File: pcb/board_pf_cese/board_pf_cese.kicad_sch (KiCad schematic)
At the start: 13 parts, among them J1 Screw_Terminal_01x02, J2 Conn_01x04, J3 Conn_01x04, J4 Conn_01x04, J5 Conn_01x04, J6 Conn_01x15, J7 Conn_01x15, J8 Conn_01x08, J9 Conn_01x08

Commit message: colocacion de componentes en el pcb
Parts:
- D1, D2: footprint (none) -> LED_THT:LED_D3.0mm
- J1: footprint (none) -> TerminalBlock_Phoenix:TerminalBlock_Phoenix_MPT-0,5-2-2.54_1x02_P2.54mm_Horizontal
- J2, J3, J4, J5: footprint (none) -> Connector_PinSocket_2.54mm:PinSocket_1x04_P2.54mm_Vertical
- J6, J7: footprint (none) -> Connector_PinSocket_2.54mm:PinSocket_1x15_P2.54mm_Vertical
- J8, J9: footprint (none) -> Connector_PinSocket_2.54mm:PinSocket_1x08_P2.54mm_Vertical
- R1, R2: footprint (none) -> Resistor_THT:R_Axial_DIN0207_L6.3mm_D2.5mm_P10.16mm_Horizontal
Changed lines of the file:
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@@
     (property "Reference" "J3" (id 0) (at 52.07 105.41 0))
     (property "Value" "Conn_01x04" (id 1) (at 52.07 107.95 0))
-    (property "Footprint" "" (id 2) (at 52.07 114.3 0)
+    (property "Footprint" "Connector_PinSocket_2.54mm:PinSocket_1x04_P2.54mm_Vertical" (id 2) (at 52.07 114.3 0)
       (effects (font (size 1.27 1.27)) hide)
     )
@@
     (property "Reference" "J5" (id 0) (at 52.07 153.67 0))
     (property "Value" "Conn_01x04" (id 1) (at 52.07 156.21 0))
-    (property "Footprint" "" (id 2) (at 52.07 162.56 0)
+    (property "Footprint" "Connector_PinSocket_2.54mm:PinSocket_1x04_P2.54mm_Vertical" (id 2) (at 52.07 162.56 0)
       (effects (font (size 1.27 1.27)) hide)
     )
@@
     (property "Reference" "J9" (id 0) (at 247.65 35.56 0))
     (property "Value" "Conn_01x08" (id 1) (at 247.65 38.1 0))
-    (property "Footprint" "" (id 2) (at 247.65 49.53 0)
+    (property "Footprint" "Connector_PinSocket_2.54mm:PinSocket_1x08_P2.54mm_Vertical" (id 2) (at 247.65 49.53 0)
       (effects (font (size 1.27 1.27)) hide)
     )
@@
     (property "Reference" "J1" (id 0) (at 38.1 34.29 0))
     (property "Value" "Screw_Terminal_01x02" (id 1) (at 38.1 36.83 0))
-    (property "Footprint" "" (id 2) (at 38.1 40.64 0)
+    (property "Footprint" "TerminalBlock_Phoenix:TerminalBlock_Phoenix_MPT-0,5-2-2.54_1x02_P2.54mm_Horizontal" (id 2) (at 38.1 40.64 0)
       (effects (font (size 1.27 1.27)) hide)
     )
@@
     (property "Reference" "J4" (id 0) (at 52.07 129.54 0))
     (property "Value" "Conn_01x04" (id 1) (at 52.07 132.08 0))
-    (property "Footprint" "" (id 2) (at 52.07 137.16 0)
+    (property "Footprint" "Connector_PinSocket_2.54mm:PinSocket_1x04_P2.54mm_Vertical" (id 2) (at 52.07 137.16 0)
       (effects (font (size 1.27 1.27)) hide)
     )
@@
       (effects (font (size 1.27 1.27)) (justify left))
     )
-    (property "Footprint" "" (id 2) (at 134.62 62.23 0)
+    (property "Footprint" "Connector_PinSocket_2.54mm:PinSocket_1x15_P2.54mm_Vertical" (id 2) (at 134.62 62.23 0)
       (effects (font (size 1.27 1.27)) hide)
     )
@@
       (effects (font (size 1.27 1.27)) (justify left))
     )
-    (property "Footprint" "" (id 2) (at 229.87 49.53 0)
+    (property "Footprint" "Connector_PinSocket_2.54mm:PinSocket_1x08_P2.54mm_Vertical" (id 2) (at 229.87 49.53 0)
       (effects (font (size 1.27 1.27)) hide)
     )
@@
     (property "Reference" "J7" (id 0) (at 149.86 38.1 0))
     (property "Value" "Conn_01x15" (id 1) (at 149.86 40.64 0))
-    (property "Footprint" "" (id 2) (at 149.86 62.23 0)
+    (property "Footprint" "Connector_PinSocket_2.54mm:PinSocket_1x15_P2.54mm_Vertical" (id 2) (at 149.86 62.23 0)
       (effects (font (size 1.27 1.27)) hide)
     )
@@
       (effects (font (size 1.27 1.27)) (justify right))
     )
-    (property "Footprint" "" (id 2) (at 231.14 123.19 0)
+    (property "Footprint" "LED_THT:LED_D3.0mm" (id 2) (at 231.14 123.19 0)
       (effects (font (size 1.27 1.27)) hide)
     )
@@
       (effects (font (size 1.27 1.27)) (justify left))
     )
-    (property "Footprint" "" (id 2) (at 229.362 111.76 90)
+    (property "Footprint" "Resistor_THT:R_Axial_DIN0207_L6.3mm_D2.5mm_P10.16mm_Horizontal" (id 2) (at 229.362 111.76 90)
       (effects (font (size 1.27 1.27)) hide)
     )
@@
     (property "Reference" "J2" (id 0) (at 52.07 81.28 0))
     (property "Value" "Conn_01x04" (id 1) (at 52.07 83.82 0))
-    (property "Footprint" "" (id 2) (at 52.07 90.17 0)
+    (property "Footprint" "Connector_PinSocket_2.54mm:PinSocket_1x04_P2.54mm_Vertical" (id 2) (at 52.07 90.17 0)
       (effects (font (size 1.27 1.27)) hide)
     )
@@
       (effects (font (size 1.27 1.27)) (justify right))
     )
-    (property "Footprint" "" (id 2) (at 245.11 123.19 0)
+    (property "Footprint" "LED_THT:LED_D3.0mm" (id 2) (at 245.11 123.19 0)
       (effects (font (size 1.27 1.27)) hide)
     )
@@
       (effects (font (size 1.27 1.27)) (justify left))
     )
-    (property "Footprint" "" (id 2) (at 243.332 111.76 90)
+    (property "Footprint" "Resistor_THT:R_Axial_DIN0207_L6.3mm_D2.5mm_P10.16mm_Horizontal" (id 2) (at 243.332 111.76 90)
       (effects (font (size 1.27 1.27)) hide)
     )
@@
     )
     (path "/c2c16862-67ff-42a4-afba-5ce90d66562f"
-      (reference "D1") (unit 1) (value "LED") (footprint "")
+      (reference "D1") (unit 1) (value "LED") (footprint "LED_THT:LED_D3.0mm")
     )
     (path "/dbc81720-7b11-4359-846d-7205cd8fe101"
-      (reference "D2") (unit 1) (value "LED") (footprint "")
+      (reference "D2") (unit 1) (value "LED") (footprint "LED_THT:LED_D3.0mm")
     )
     (path "/587a09bb-470b-457f-a0a3-250ad0d2fb36"
-      (reference "J1") (unit 1) (value "Screw_Terminal_01x02") (footprint "")
+      (reference "J1") (unit 1) (value "Screw_Terminal_01x02") (footprint "TerminalBlock_Phoenix:TerminalBlock_Phoenix_MPT-0,5-2-2.54_1x02_P2.54mm_Horizontal")
     )
     (path "/d8bb4505-4a60-4c8e-93d0-f0d006cbd6be"
-      (reference "J2") (unit 1) (value "Conn_01x04") (footprint "")
+      (reference "J2") (unit 1) (value "Conn_01x04") (footprint "Connector_PinSocket_2.54mm:PinSocket_1x04_P2.54mm_Vertical")
     )
     (path "/10d63046-38df-4d8c-a6ed-2c840220c859"
-      (reference "J3") (unit 1) (value "Conn_01x04") (footprint "")
+      (reference "J3") (unit 1) (value "Conn_01x04") (footprint "Connector_PinSocket_2.54mm:PinSocket_1x04_P2.54mm_Vertical")
     )
     (path "/6a61e119-9f63-4329-8362-52b2b0488a19"
-      (reference "J4") (unit 1) (value "Conn_01x04") (footprint "")
+      (reference "J4") (unit 1) (value "Conn_01x04") (footprint "Connector_PinSocket_2.54mm:PinSocket_1x04_P2.54mm_Vertical")
     )
     (path "/36055566-6b01-4db2-9bbc-8bfca51561a0"
-      (reference "J5") (unit 1) (value "Conn_01x04") (footprint "")
+      (reference "J5") (unit 1) (value "Conn_01x04") (footprint "Connector_PinSocket_2.54mm:PinSocket_1x04_P2.54mm_Vertical")
     )
     (path "/97707070-82f5-4b99-9a61-dd439405b8e4"
-      (reference "J6") (unit 1) (value "Conn_01x15") (footprint "")
+      (reference "J6") (unit 1) (value "Conn_01x15") (footprint "Connector_PinSocket_2.54mm:PinSocket_1x15_P2.54mm_Vertical")
     )
     (path "/b19ccc00-1834-4ad9-8a41-194837d21601"
-      (reference "J7") (unit 1) (value "Conn_01x15") (footprint "")
+      (reference "J7") (unit 1) (value "Conn_01x15") (footprint "Connector_PinSocket_2.54mm:PinSocket_1x15_P2.54mm_Vertical")
     )
     (path "/9785fda7-cab3-4d47-9212-e11d694f5957"
-      (reference "J8") (unit 1) (value "Conn_01x08") (footprint "")
+      (reference "J8") (unit 1) (value "Conn_01x08") (footprint "Connector_PinSocket_2.54mm:PinSocket_1x08_P2.54mm_Vertical")
     )
     (path "/49eaddac-835c-4189-b730-464b8007ff04"
-      (reference "J9") (unit 1) (value "Conn_01x08") (footprint "")
+      (reference "J9") (unit 1) (value "Conn_01x08") (footprint "Connector_PinSocket_2.54mm:PinSocket_1x08_P2.54mm_Vertical")
     )
     (path "/caddb6f5-1981-41a3-8e50-483141adabfe"
-      (reference "R1") (unit 1) (value "R") (footprint "")
+      (reference "R1") (unit 1) (value "R") (footprint "Resistor_THT:R_Axial_DIN0207_L6.3mm_D2.5mm_P10.16mm_Horizontal")
     )
     (path "/f10d6887-62d2-486c-8b5f-1063e4909e37"
-      (reference "R2") (unit 1) (value "R") (footprint "")
-    )
-  )
+      (reference "R2") (unit 1) (value "R") (footprint "Resistor_THT:R_Axial_DIN0207_L6.3mm_D2.5mm_P10.16mm_Horizontal")
+    )
+  )

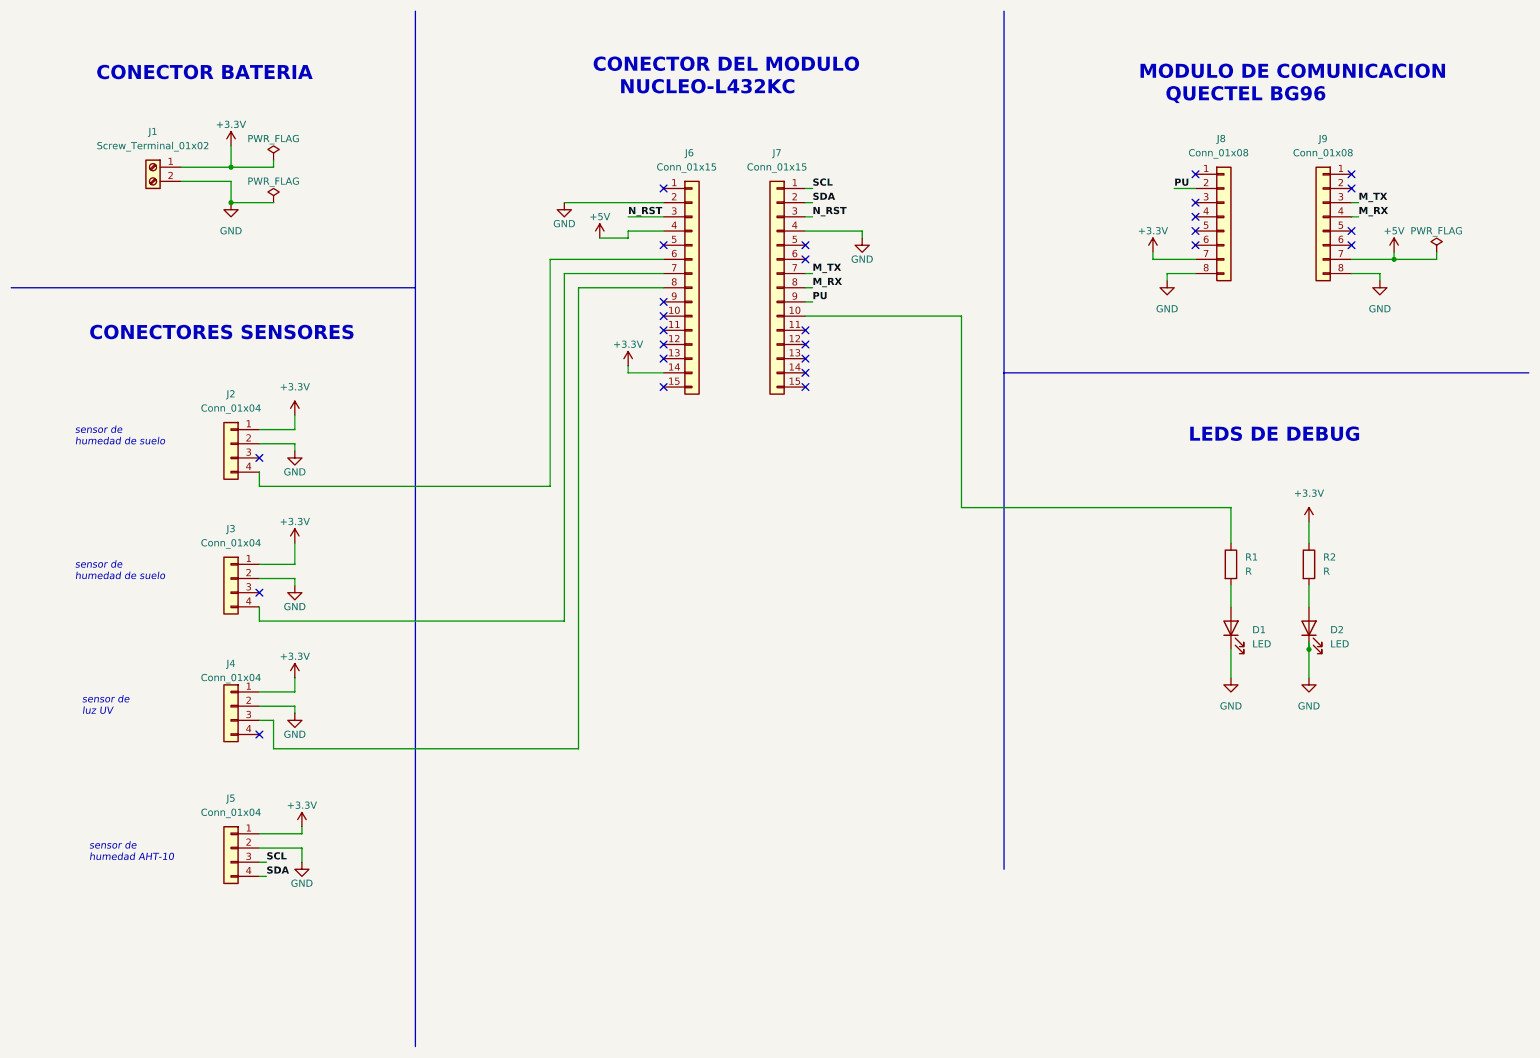
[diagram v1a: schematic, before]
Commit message: se redimensiono el tamaño del pcb
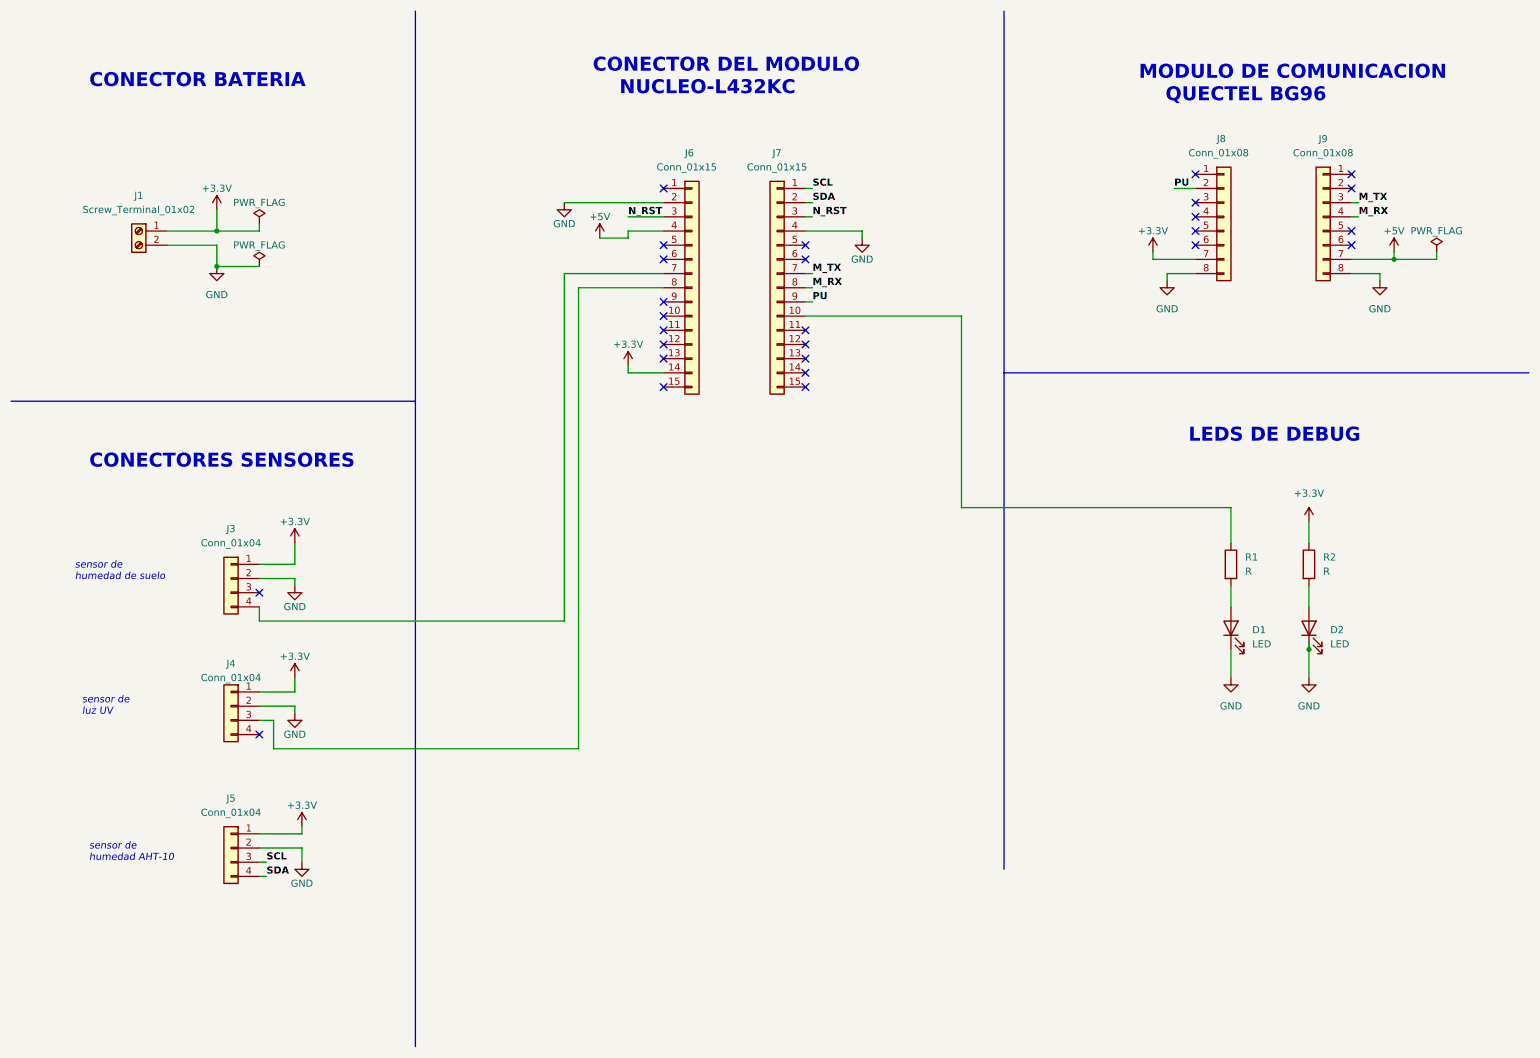
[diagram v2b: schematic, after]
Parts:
- removed J2: Conn_01x04, Connector_PinSocket_2.54mm:PinSocket_1x04_P2.54mm_Vertical, symbol Connector_Generic:Conn_01x04
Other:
- moved on the sheet: J1

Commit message: ruteo con errores
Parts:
- added J2: Conn_01x04, Connector_PinSocket_2.54mm:PinSocket_1x04_P2.54mm_Vertical, symbol Connector_Generic:Conn_01x04
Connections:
- net +3.3V: now also J2.1 (Pin_1); no longer R2.1
- net GND: now also J2.2 (Pin_2)
- net M_RX: now also J7.2 (Pin_2); no longer J7.8 (Pin_8)
- net M_TX: now also J7.1 (Pin_1); no longer J7.7 (Pin_7)
- net SCL: now also J6.6 (Pin_6); no longer J7.1 (Pin_1)
- net SDA: now also J7.15 (Pin_15); no longer J7.2 (Pin_2)
- net at J3.4 (Pin_4): now also J6.8 (Pin_8); no longer J6.7 (Pin_7)
- net at J4.3 (Pin_3): now also J6.10 (Pin_10); no longer J6.8 (Pin_8)
- net at J6.9 (Pin_9): now also J2.4 (Pin_4)
- net at J7.10 (Pin_10): no longer R1.1
- net SE: now reaches J7.13 (Pin_13)
- net SE: now also R2.1
- net OR: now reaches J7.5 (Pin_5)
- net OR: now also J8.2 (Pin_2)
- net SO: now reaches J7.6 (Pin_6)
- net SO: now also R1.1
- net +5V: no longer names the net of J9.7 (Pin_7)
- net +5V: no longer J6.4 (Pin_4)
- net N_RST: no longer names the net of J6.3 (Pin_3)
- net N_RST: no longer J7.3 (Pin_3)
- net PU: no longer names the net of J7.9 (Pin_9)
- net PU: no longer J8.2 (Pin_2)
- no-connect marks 27 -> 30
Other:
- note added: "sensor de humedad de suelo 2"
- moved on the sheet: D1, D2, J3, J4, J5, J6, J7, J8, J9, R1, R2

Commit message: se actualizo el metodo de alimentacion
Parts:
- added J10: Screw_Terminal_01x02, TerminalBlock_Phoenix:TerminalBlock_Phoenix_MPT-0,5-2-2.54_1x02_P2.54mm_Horizontal, symbol Connector:Screw_Terminal_01x02
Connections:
- net +3.3V: no longer J1.1 (Pin_1)
- net GND: now also J10.2 (Pin_2)
- net M_RX: now also J7.1 (Pin_1); no longer J7.2 (Pin_2)
- net M_TX: now also J7.2 (Pin_2); no longer J7.1 (Pin_1)
- net +5V: now reaches J9.7 (Pin_7)
- net +5V: now also J1.1 (Pin_1)
- net +12V: now reaches J6.1 (Pin_1)
- net +12V: now also J10.1 (Pin_1)
- no-connect marks 30 -> 28
